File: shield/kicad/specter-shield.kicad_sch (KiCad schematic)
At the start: 0 parts

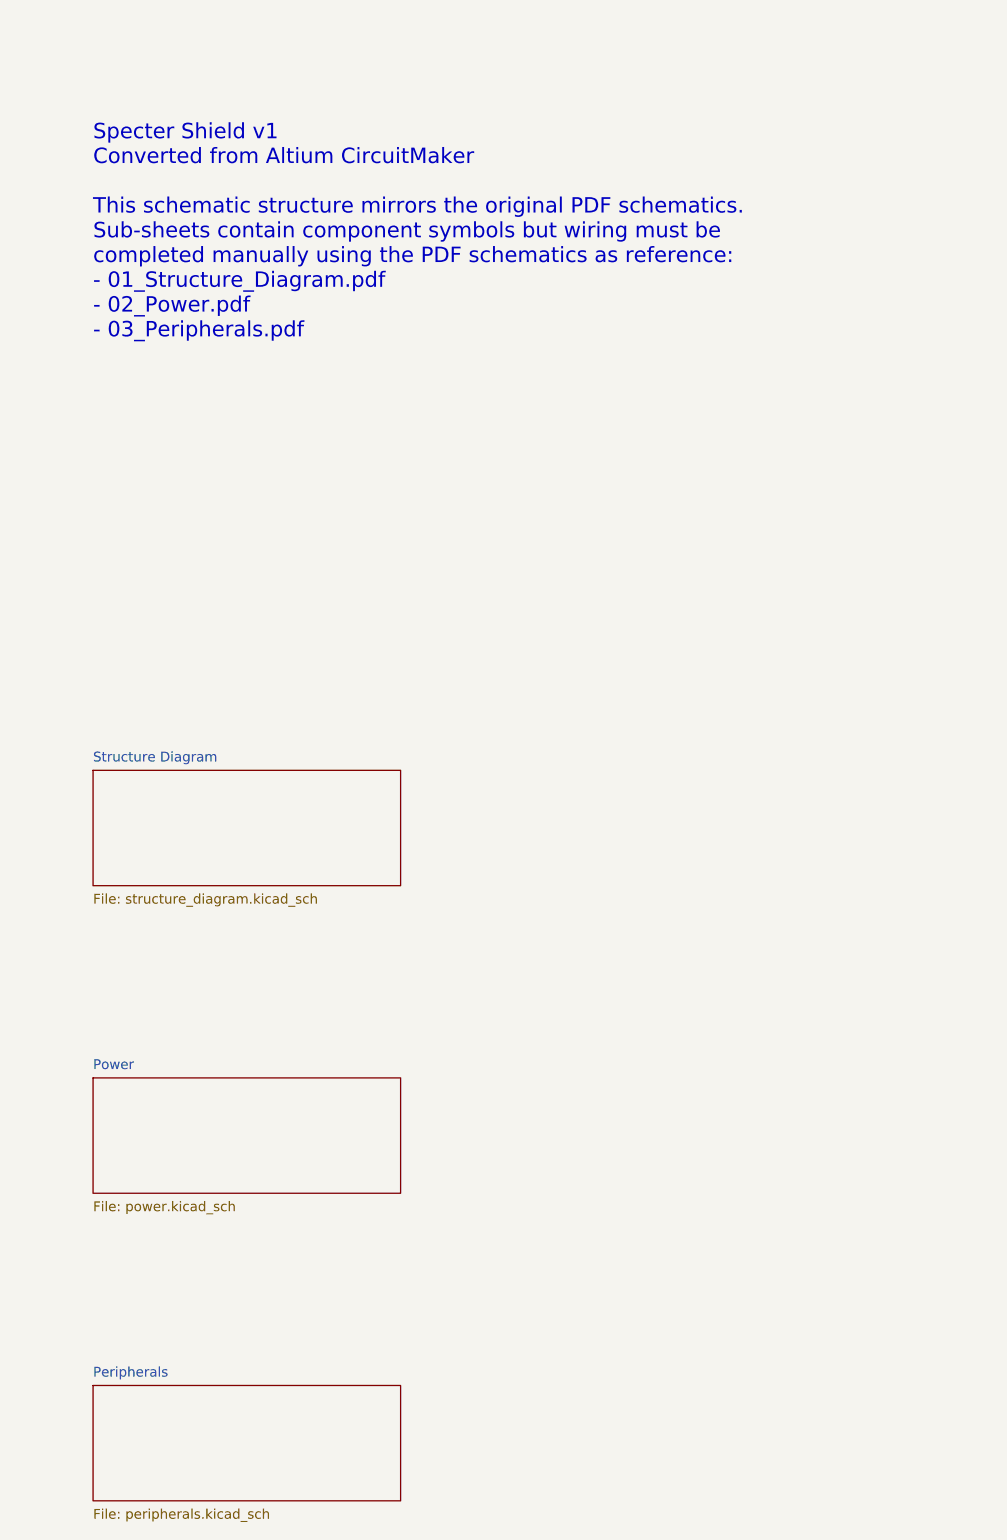
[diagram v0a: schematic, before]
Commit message: Complete schematic wiring, footprint assignments, and validation renders
- Generated proper KiCad symbols with pin definitions for all 139 components
- Created 2 hierarchical sub-sheets: Power Supply and Peripherals & Connectors
- Added schematic wiring with net labels (VBUS, VBAT, V3V3, GND, I2C, SPI, etc.)
- Assigned KiCad standard library footprints to all components
- Rendered schematic and PCB SVGs using kicad-cli-nightly
- Ran ERC and DRC validation
- Updated README with rendered images and footprint assignment table

Agent-Logs-Url: https://github.com/3rdIteration/specter-diy/sessions/67aa0d59-b533-4f87-a3fd-0109cc63ae2b

Co-authored-by: 3rdIteration <2230318+3rdIteration@users.noreply.github.com>
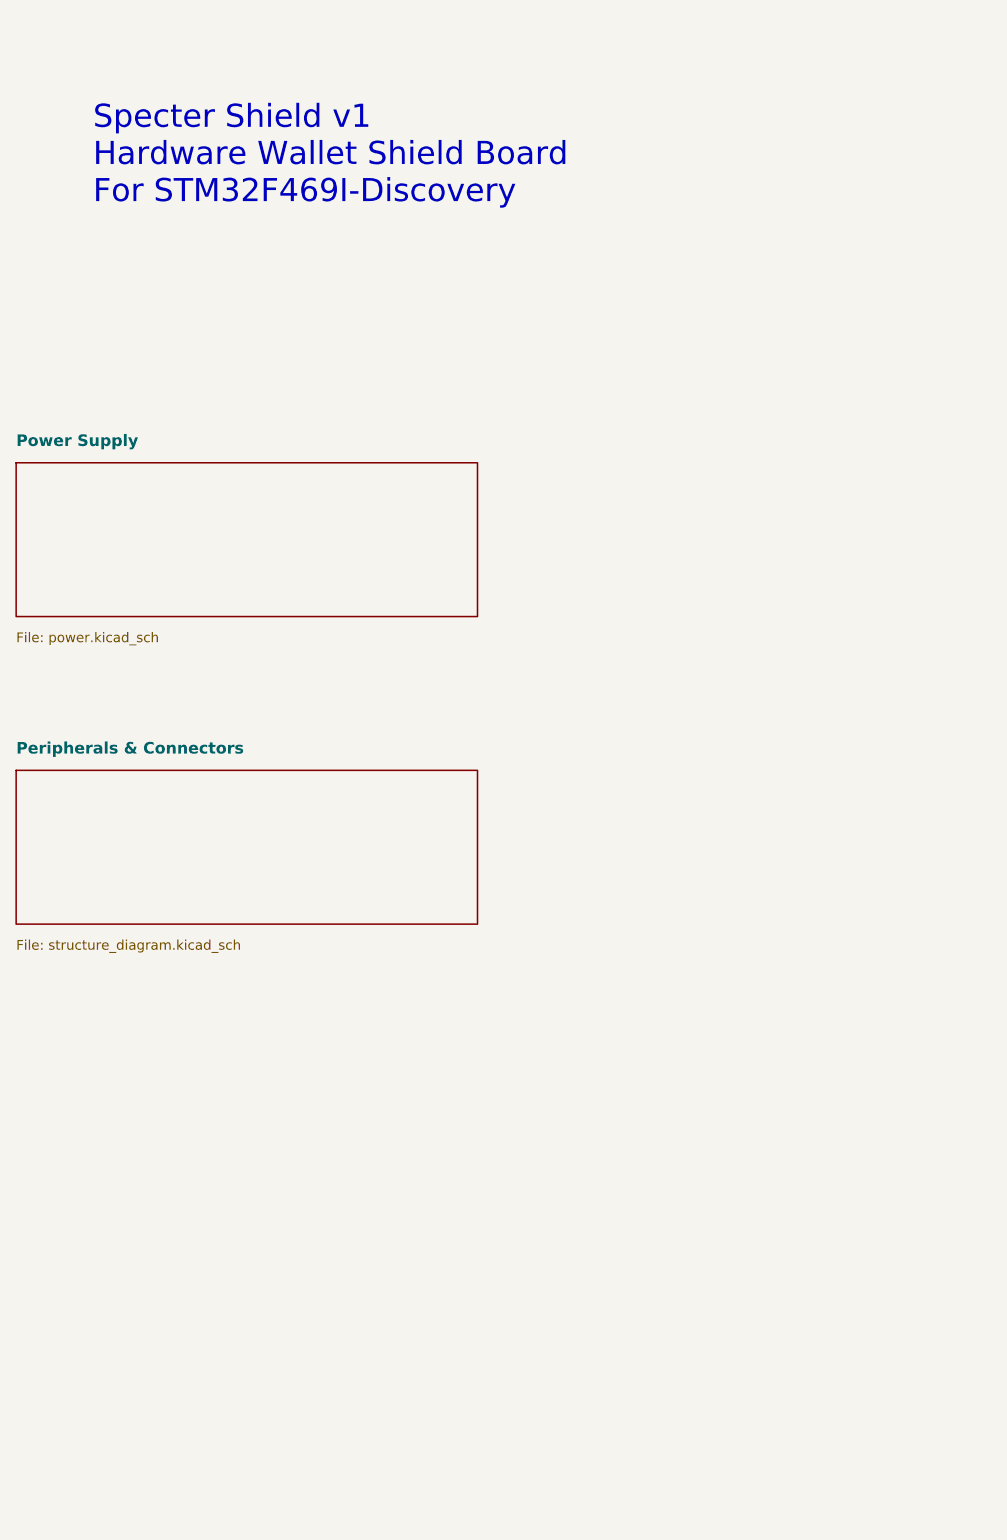
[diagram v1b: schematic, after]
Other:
- removed sheet Peripherals
- removed sheet Power
- removed sheet Structure Diagram
- added sheet Peripherals & Connectors (structure_diagram.kicad_sch)
- added sheet Power Supply (power.kicad_sch)
- note added: "Specter Shield v1 Hardware Wallet Shield Board For STM32F469I-Discovery"
- note removed: "Specter Shield v1 Converted from Altium CircuitMaker This schematic structure mirrors the original PDF schematics. Sub-sheets contain component symbols but wiring must be completed manually using the PDF schematics as reference: - 01_Structure_Diagram.pdf - 02_Power.pdf - 03_Peripherals.pdf"
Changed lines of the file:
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@@
 (kicad_sch
 	(version 20231120)
-	(generator "specter-shield-converter")
-	(generator_version "1.0")
+	(generator "specter-shield-builder")
+	(generator_version "2.0")
 	(paper "A3")
 	(title_block
 		(title "Specter Shield v1")
-		(comment 1 "Converted from Altium CircuitMaker")
-		(comment 2 "Schematic structure only - wiring needs manual completion")
+		(comment 1 "KiCad conversion from Altium CircuitMaker")
+		(comment 2 "github.com/3rdIteration/specter-diy")
 	)
-	(text "Specter Shield v1\nConverted from Altium CircuitMaker\n\nThis schematic structure mirrors the original PDF schematics.\nSub-sheets contain component symbols but wiring must be\ncompleted manually using the PDF schematics as reference:\n- 01_Structure_Diagram.pdf\n- 02_Power.pdf\n- 03_Peripherals.pdf"
-		(exclude_from_sim no) (at 50 50 0)
-		(effects (font (size 2 2)) (justify left))
+	(text "Specter Shield v1\nHardware Wallet Shield Board\nFor STM32F469I-Discovery"
+		(exclude_from_sim no)
+		(at 50 40 0)
+		(effects (font (size 3 3)) (justify left))
 	)
-	(sheet (at 50 120) (size 40 15)
-		(stroke (width 0.1) (type solid) (color 0 0 0 0))
-		(fill (color 255 255 255 0.0))
-		(property "Sheetname" "Structure Diagram" (at 50 119 0)
-			(effects (font (size 1.27 1.27)) (justify left bottom)))
-		(property "Sheetfile" "structure_diagram.kicad_sch" (at 50 136 0)
+	(sheet
+		(at 40 80)
+		(size 60 20)
+		(stroke (width 0.2) (type solid) (color 0 0 0 1))
+		(fill (color 255 255 230 1.0))
+		(property "Sheetname" "Power Supply"
+			(at 40 78 0)
+			(effects (font (size 1.5 1.5) bold) (justify left bottom)))
+		(property "Sheetfile" "power.kicad_sch"
+			(at 40 102 0)
 			(effects (font (size 1.27 1.27)) (justify left top)))
+		(instances
+			(project ""
+				(path "/0edde069-4094-4249-98aa-f396abbdb468"
+					(page "2"))))
 	)
-	(sheet (at 50 160) (size 40 15)
-		(stroke (width 0.1) (type solid) (color 0 0 0 0))
-		(fill (color 255 255 255 0.0))
-		(property "Sheetname" "Power" (at 50 159 0)
-			(effects (font (size 1.27 1.27)) (justify left bottom)))
-		(property "Sheetfile" "power.kicad_sch" (at 50 176 0)
+	(sheet
+		(at 40 120)
+		(size 60 20)
+		(stroke (width 0.2) (type solid) (color 0 0 0 1))
+		(fill (color 230 255 230 1.0))
+		(property "Sheetname" "Peripherals & Connectors"
+			(at 40 118 0)
+			(effects (font (size 1.5 1.5) bold) (justify left bottom)))
+		(property "Sheetfile" "structure_diagram.kicad_sch"
+			(at 40 142 0)
 			(effects (font (size 1.27 1.27)) (justify left top)))
-	)
-	(sheet (at 50 200) (size 40 15)
-		(stroke (width 0.1) (type solid) (color 0 0 0 0))
-		(fill (color 255 255 255 0.0))
-		(property "Sheetname" "Peripherals" (at 50 199 0)
-			(effects (font (size 1.27 1.27)) (justify left bottom)))
-		(property "Sheetfile" "peripherals.kicad_sch" (at 50 216 0)
-			(effects (font (size 1.27 1.27)) (justify left top)))
+		(instances
+			(project ""
+				(path "/0edde069-4094-4249-98aa-f396abbdb468"
+					(page "3"))))
 	)
 )

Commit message: Add descriptive text blocks to all schematic sheets describing functional blocks
- Main sheet: board overview, sub-sheet summaries, and design notes
- Power sheet: USB input, charger, fuel gauge, buck-boost, supervisor, power control descriptions
- Peripherals sheet: smartcard, QR scanner, Arduino headers, buzzer, bypass descriptions
- Re-rendered all schematic and PCB images with kicad-cli-nightly

Agent-Logs-Url: https://github.com/3rdIteration/specter-diy/sessions/73613ef4-1004-4e39-bea0-e2793e248b2a

Co-authored-by: 3rdIteration <2230318+3rdIteration@users.noreply.github.com>
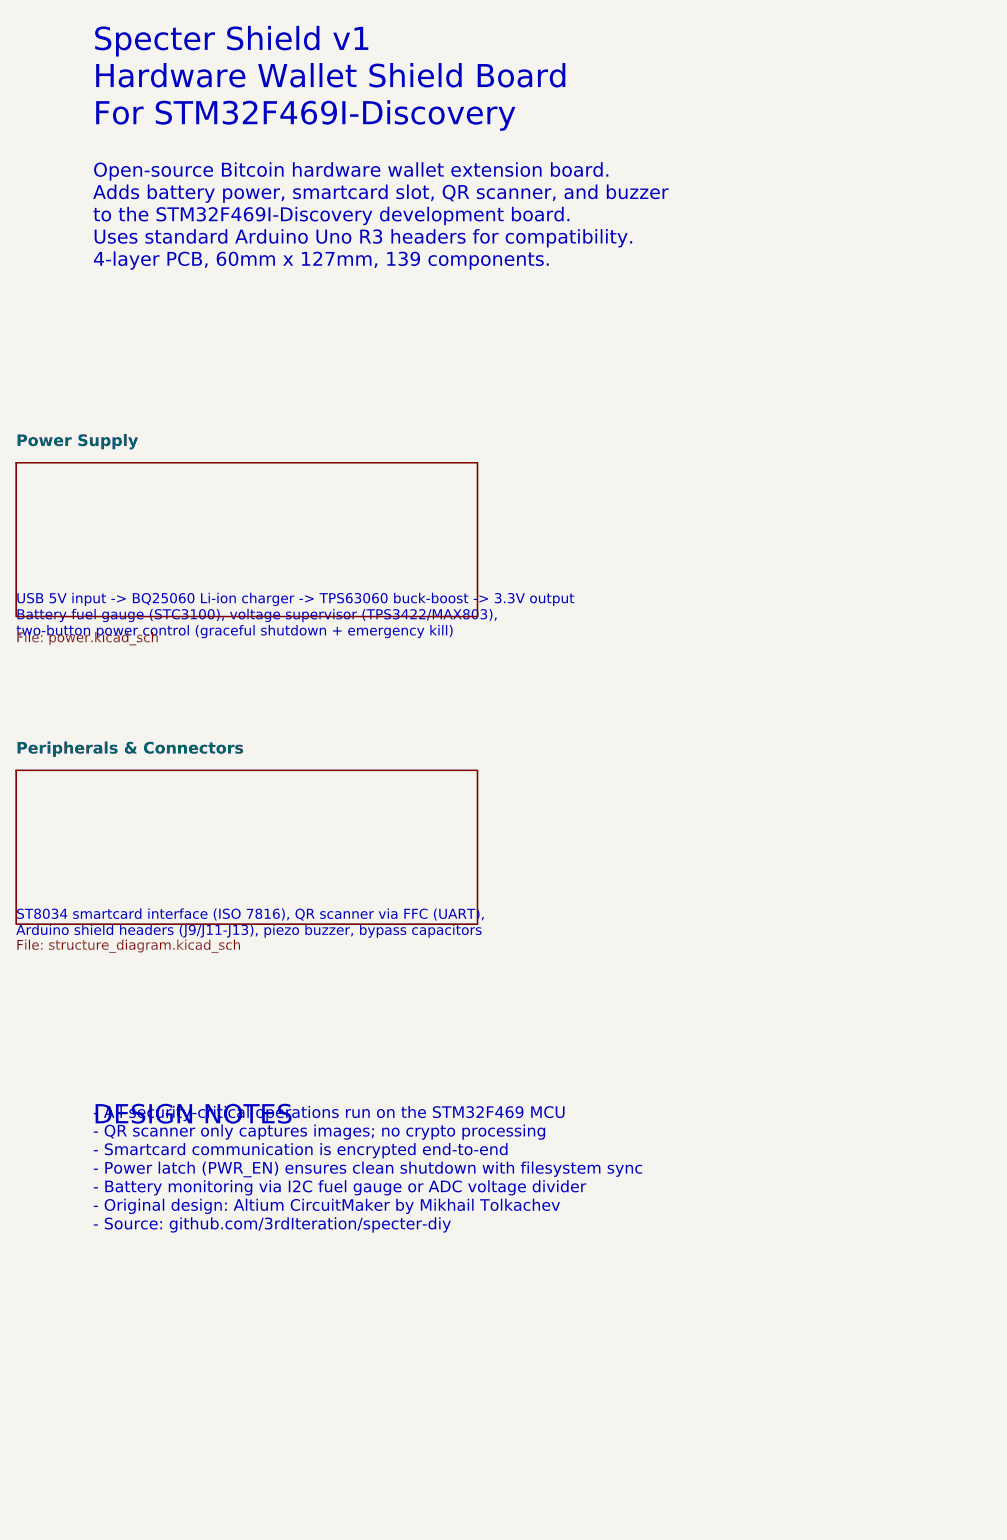
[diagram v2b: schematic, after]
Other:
- note added: "- All security-critical operations run on the STM32F469 MCU - QR scanner only captures images; no crypto processing - Smartcard communication is encrypted end-to-end - Power latch (PWR_EN) ensures clean shutdown with filesystem sync - Battery monitoring via I2C fuel gauge or ADC voltage divider - Original design: Altium CircuitMaker by Mikhail Tolkachev - Source: github.com/3rdIteration/specter-d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"
- note added: "DESIGN NOTES"
- note added: "Open-source Bitcoin hardware wallet extension board. Adds battery power, smartcard slot, QR scanner, and buzzer to the STM32F469I-Discovery development board. Uses standard Arduino Uno R3 headers for compatibility. 4-layer PCB, 60mm x 127mm, 139 components."
- note added: "ST8034 smartcard interface (ISO 7816), QR scanner via FFC (UART), Arduino shield headers (J9/J11-J13), piezo buzzer, bypass capacitors"
- note added: "USB 5V input -> BQ25060 Li-ion charger -> TPS63060 buck-boost -> 3.3V output Battery fuel gauge (STC3100), voltage supervisor (TPS3422/MAX803), two-button power control (graceful shutdown + emergency kill)"
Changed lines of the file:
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@@
 		(comment 2 "github.com/3rdIteration/specter-diy")
-	)
-	(text "Specter Shield v1\nHardware Wallet Shield Board\nFor STM32F469I-Discovery"
-		(exclude_from_sim no)
-		(at 50 40 0)
-		(effects (font (size 3 3)) (justify left))
 	)
 	(sheet
@@
 					(page "3"))))
 	)
+	(text "Specter Shield v1\nHardware Wallet Shield Board\nFor STM32F469I-Discovery"
+		(exclude_from_sim no)
+		(at 50 30 0)
+		(effects
+			(font
+				(size 3 3)
+			)
+			(justify left)
+		)
+	)
+	(text "Open-source Bitcoin hardware wallet extension board.\nAdds battery power, smartcard slot, QR scanner, and buzzer\nto the STM32F469I-Discovery development board.\nUses standard Arduino Uno R3 headers for compatibility.\n4-layer PCB, 60mm x 127mm, 139 components."
+		(exclude_from_sim no)
+		(at 50 48 0)
+		(effects
+			(font
+				(size 1.8 1.8)
+				(color 0 0 150 1)
+			)
+			(justify left)
+		)
+	)
+	(text "USB 5V input -> BQ25060 Li-ion charger -> TPS63060 buck-boost -> 3.3V output\nBattery fuel gauge (STC3100), voltage supervisor (TPS3422/MAX803),\ntwo-button power control (graceful shutdown + emergency kill)"
+		(exclude_from_sim no)
+		(at 40 100 0)
+		(effects
+			(font
+				(size 1.3 1.3)
+				(color 100 100 100 1)
+			)
+			(justify left)
+		)
+	)
+	(text "ST8034 smartcard interface (ISO 7816), QR scanner via FFC (UART),\nArduino shield headers (J9/J11-J13), piezo buzzer, bypass capacitors"
+		(exclude_from_sim no)
+		(at 40 140 0)
+		(effects
+			(font
+				(size 1.3 1.3)
+				(color 100 100 100 1)
+			)
+			(justify left)
+		)
+	)
+	(text "DESIGN NOTES"
+		(exclude_from_sim no)
+		(at 50 165 0)
+		(effects
+			(font
+				(size 2.5 2.5)
+			)
+			(justify left)
+		)
+	)
+	(text "- All security-critical operations run on the STM32F469 MCU\n- QR scanner only captures images; no crypto processing\n- Smartcard communication is encrypted end-to-end\n- Power latch (PWR_EN) ensures clean shutdown with filesystem sync\n- Battery monitoring via I2C fuel gauge or ADC voltage divider\n- Original design: Altium CircuitMaker by Mikhail Tolkachev\n- Source: github.com/3rdIteration/specter-diy"
+		(exclude_from_sim no)
+		(at 50 172 0)
+		(effects
+			(font
+				(size 1.5 1.5)
+				(color 0 0 150 1)
+			)
+			(justify left)
+		)
+	)
 )
